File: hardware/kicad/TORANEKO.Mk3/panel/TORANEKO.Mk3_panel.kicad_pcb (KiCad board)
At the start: 2 copper layers, 60 x 22.5 mm, 19 parts, among them IC5 AS5047P-ATSM, IC5_2 AS5047P-ATSM, IC5_3 AS5047P-ATSM, IC7 AS5047P-ATSM, IC7_2 AS5047P-ATSM, IC7_3 AS5047P-ATSM, U3 Encord, U3_2 Encord, U3_3 Encord, U5 Encord, U5_2 Encord, U5_3 Encord

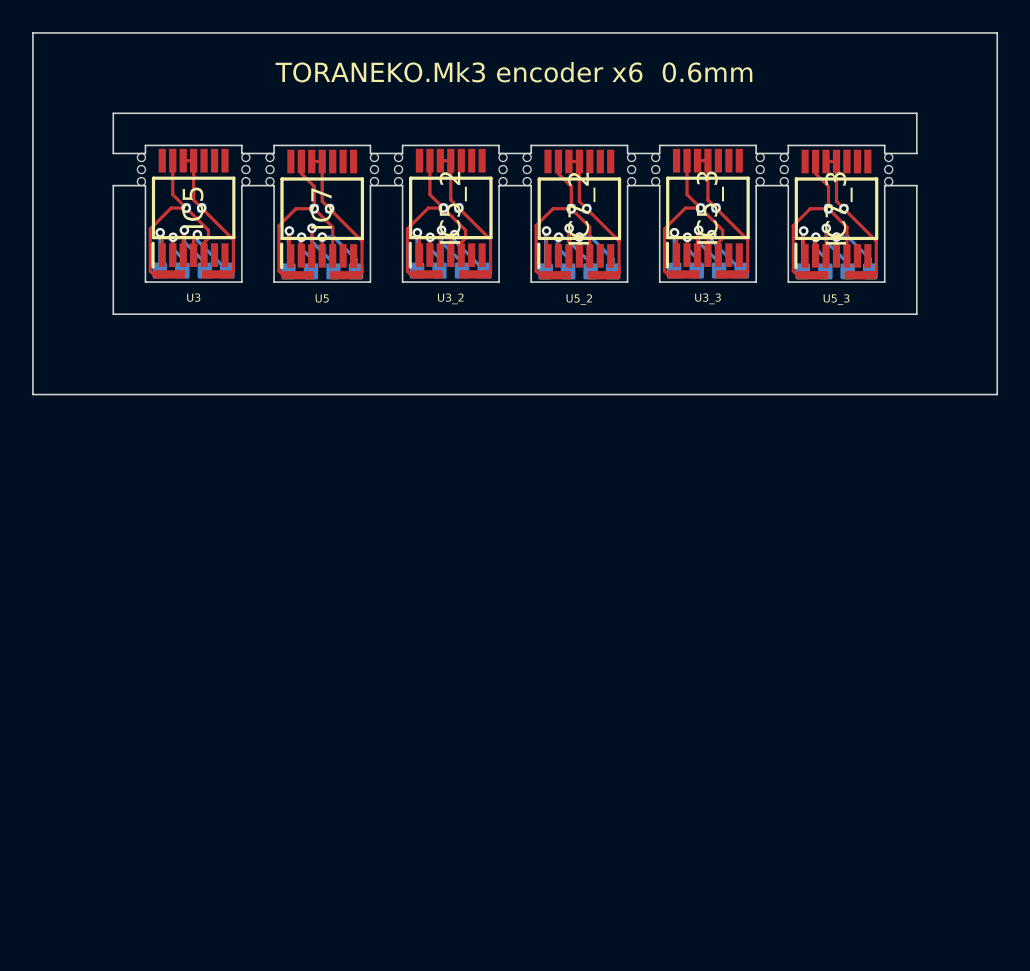
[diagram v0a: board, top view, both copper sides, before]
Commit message: Add upper fixing plate to the order panel (60 x 56.3mm)
Rename encoder panel to TORANEKO.Mk3_panel / make_panel.py. The plate
outline, cutouts and holes are read from 上部固定基板外形.dxf; tabs only on
its straight edges, separated from the encoder row by a 3mm bar.

Co-Authored-By: Claude Opus 5.5 <noreply@anthropic.com>
Claude-Session: https://claude.ai/code/session_01Cv6KpZe6NLHWQTjQMUz9Sg
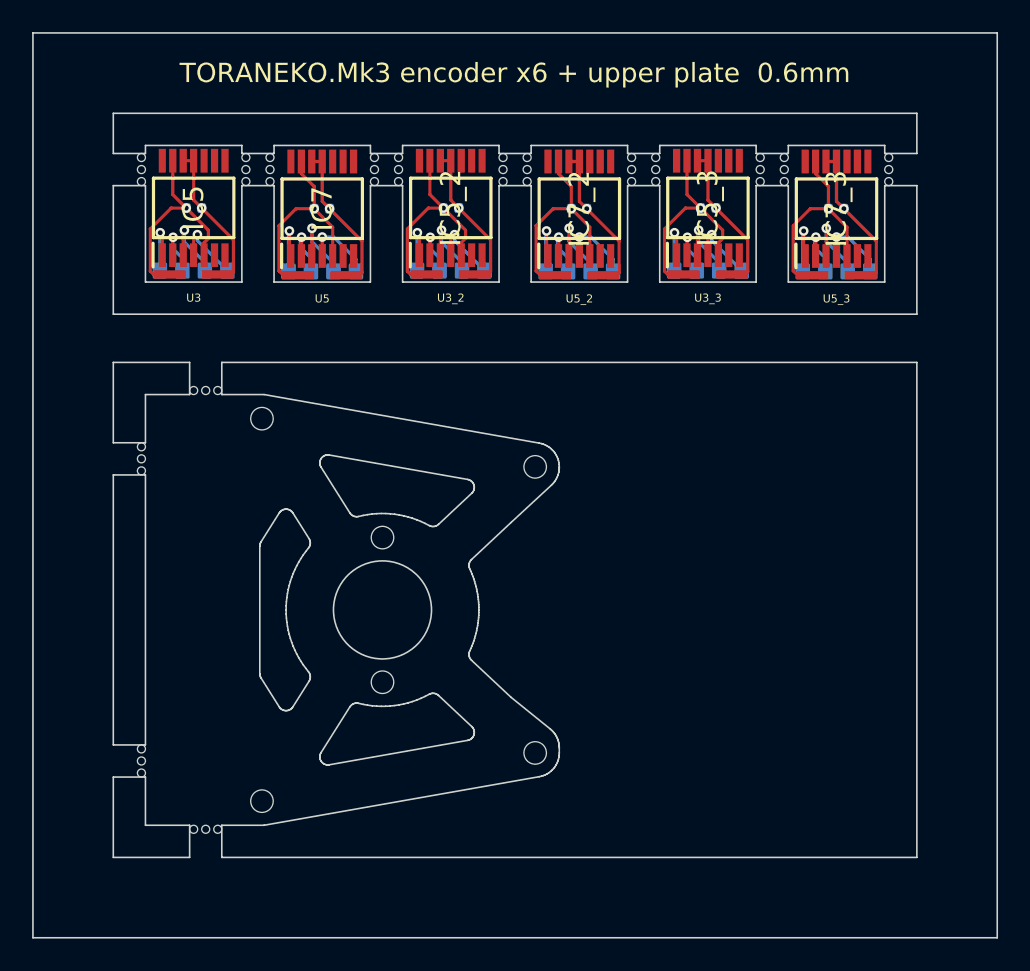
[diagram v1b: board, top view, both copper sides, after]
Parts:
- added H101: UpperPlateHoles, TORANEKO_Panel:UpperPlateHoles, F.Cu at (0.00, 0.00)
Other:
- board size 60 x 22.5 mm -> 60 x 56.3 mm
- board text added: "TORANEKO.Mk3 encoder x6 + upper plate 0.6mm"
- board text removed: "TORANEKO.Mk3 encoder x6 0.6mm"

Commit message: Panel: add logo silkscreen on the upper plate; follow moved encoder boards
- Place ロゴ_ホワイトグリント.dxf as filled F.SilkS polygons in the lower-left
  free area of the upper plate (largest fit, 0.3mm clearance -> 7.1mm wide)
- Update encoder board outline coordinates to the new main-board positions

Co-Authored-By: Claude Opus 5.5 <noreply@anthropic.com>
Claude-Session: https://claude.ai/code/session_01Cv6KpZe6NLHWQTjQMUz9Sg
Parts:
- added LOGO1: WhiteGlint, TORANEKO_Panel:Logo, F.Cu at (0.00, 0.00)
